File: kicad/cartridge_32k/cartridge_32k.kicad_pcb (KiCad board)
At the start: 2 copper layers, 39 x 66 mm, 8 parts, among them J1 Card edge (87715-9106 mate), U1 ATF22V10C-7PX, U2 AT28C256-15PU, U3 AS7C256C-15PCN

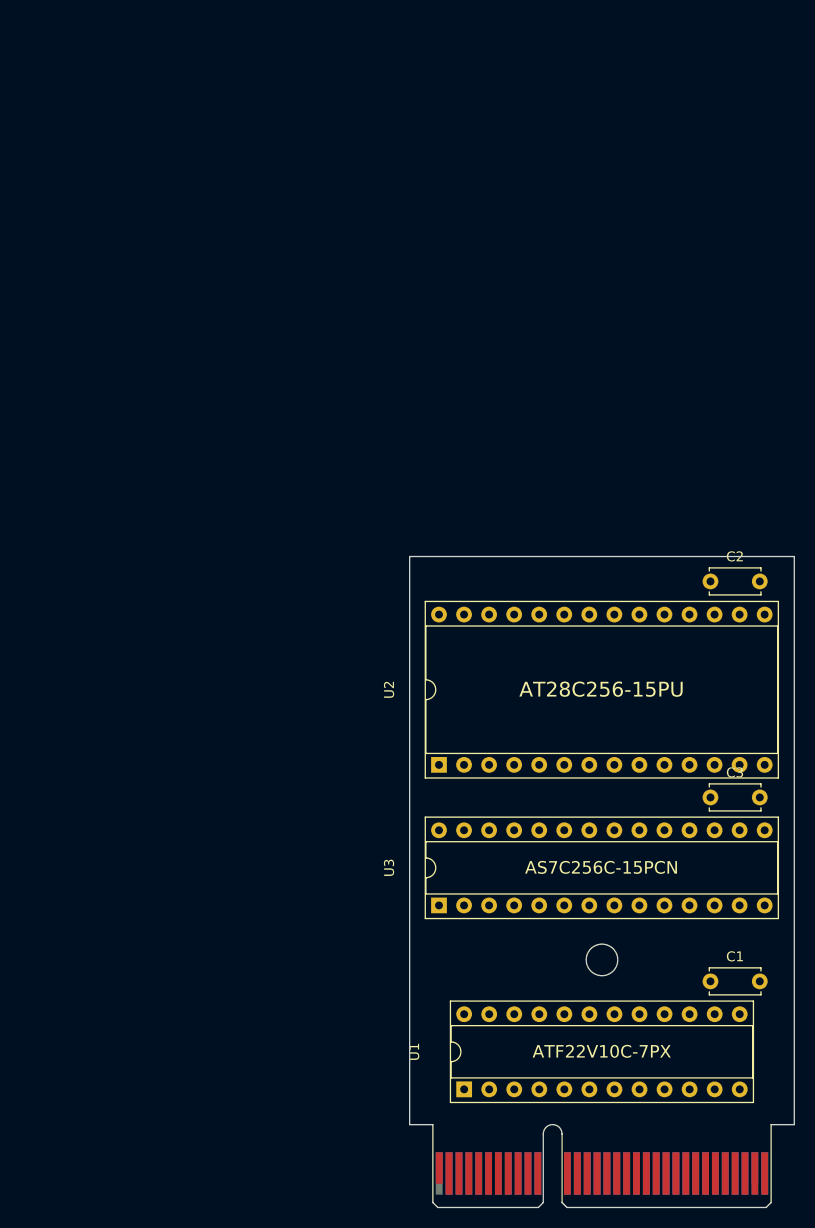
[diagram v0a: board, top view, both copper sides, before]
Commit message: 32K cartridge layout from Justin's local copy; main board zones refilled
- cartridge_32k: Justin's placement (J1, U1, U2, C1-C3, H1) and the
  KiCad 9 project settings it was saved with.
- placard.kicad_pcb: zones refilled in KiCad 9.0.6. 26 teardrops still
  carried the pre-#97 net names (SRC0-7, Net-(J8-/CART)); renamed to
  /Data bus/SRC0-7 and ~{CART} to match their net numbers. No footprint,
  track or via changes. DRC: only the 2 existing silk-over-copper warnings.

Co-Authored-By: Claude Opus 5.5 (1M context) <noreply@anthropic.com>
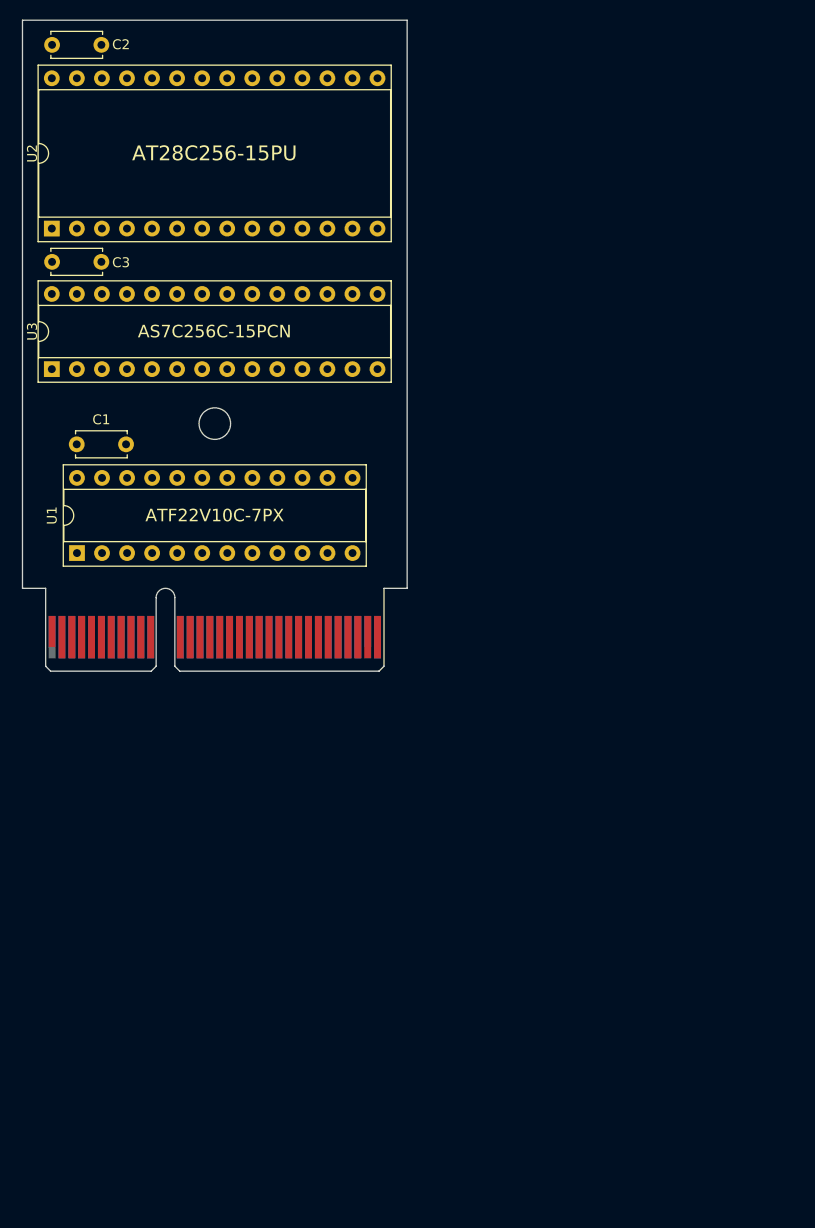
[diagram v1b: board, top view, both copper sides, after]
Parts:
- moved C2 86.1 mm to (63.7, 82.1)
- moved C3 86.1 mm to (63.7, 104.1)
- moved C1 84.2 mm to (66.2, 122.6)
- moved J1 67.1 mm to (63.7, 142.2)
- moved U1 67.1 mm to (66.3, 133.7)
- moved H1 67.1 mm to (80.2, 120.5)
- moved U2 67.1 mm to (63.7, 100.8)
- moved U3 67.1 mm to (63.7, 115.0)
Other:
- outline, holes or cut-outs redrawn

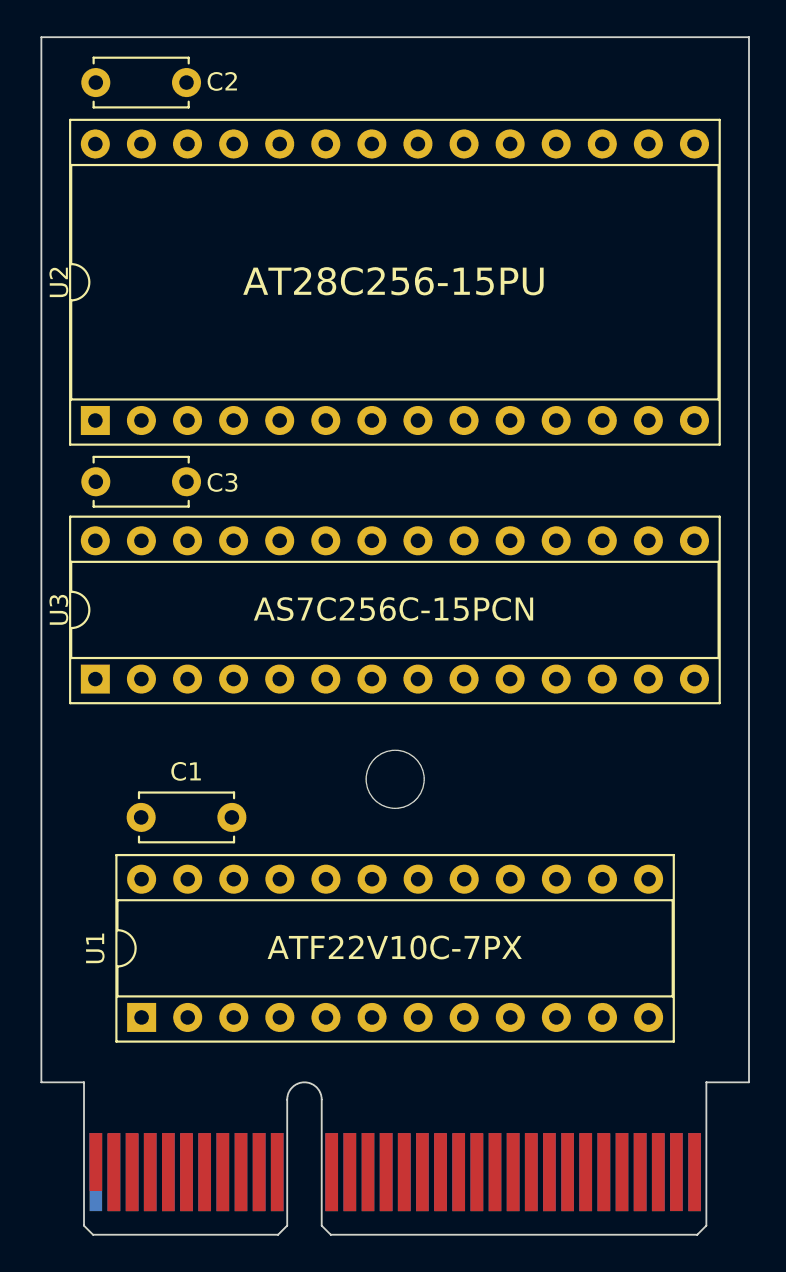
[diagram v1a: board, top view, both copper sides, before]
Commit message: Commit Justin's filled boards: routed carts, J8 reroute, J4 Hirose, library links
The three boards as Justin saved them after zone fill, teardrops and a
clean DRC (2026-10-26): both cartridges 4-layer routed, main board J8
rerouted for the new cartridge pinout, J4 swapped to the Hirose SD socket,
and every footprint linked to the placard library.

Co-Authored-By: Claude Opus 5.5 <noreply@anthropic.com>
Claude-Session: https://claude.ai/code/session_017okF1JiLRNFTfH7Az85hff
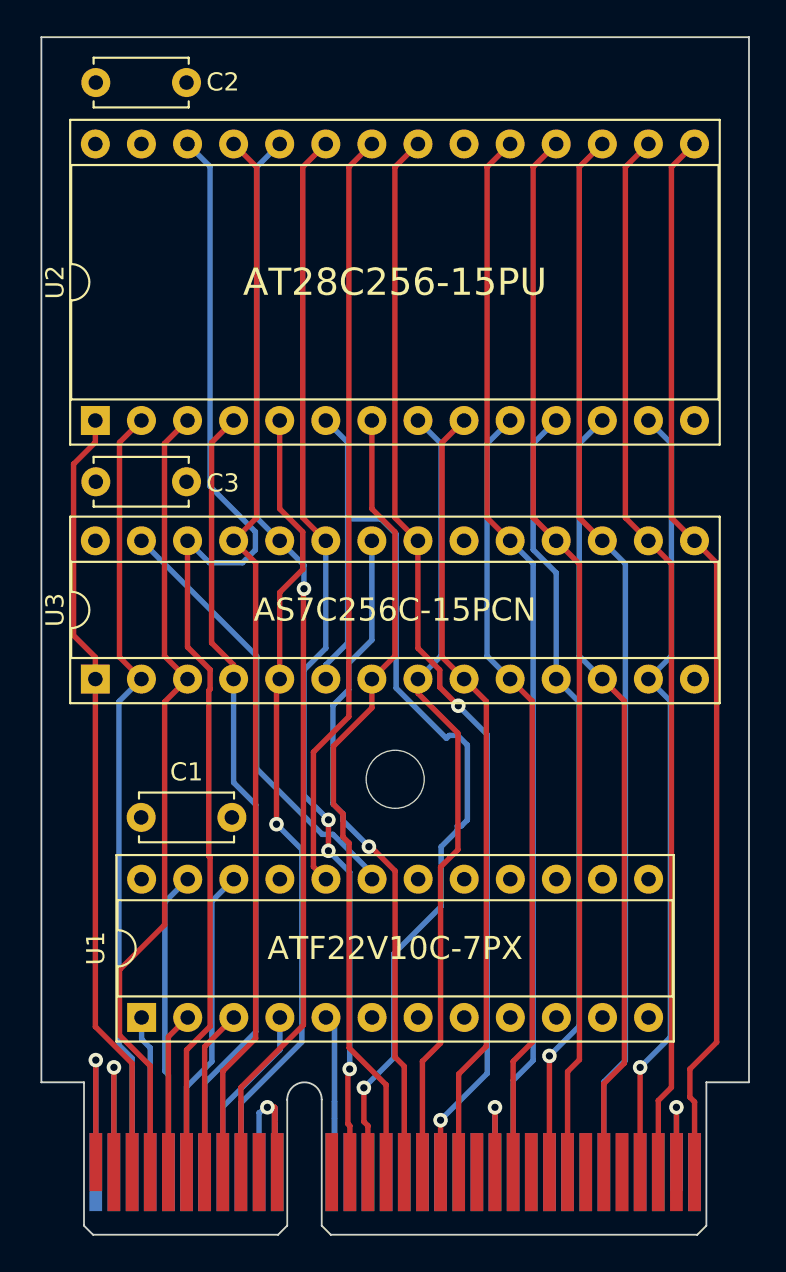
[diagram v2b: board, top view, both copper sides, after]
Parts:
- C1, C2, C3: footprint Capacitor_THT:C_Disc_D5.0mm_W2.5mm_P5.00mm -> placard:C_Disc_D5.0mm_W2.5mm_P5.00mm
- H1: footprint MountingHole:MountingHole_3.2mm_M3 -> placard:MountingHole_3.2mm_M3
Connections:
- J1 pad A10: /A14 -> (no net)
- J1 pad A12: /D0 -> (no net)
- J1 pad A13: /D2 -> /A11
- J1 pad A14: /D4 -> /A4
- J1 pad A15: /D6 -> /A3
- J1 pad A16: /~{CE_LO} -> /~{ROM_OE}
- J1 pad A17: /~{ROM_OE} -> /A2
- J1 pad A18: Net-(J1-PIXEL_ENABLE) -> /A10
- J1 pad A19: Net-(J1-RUN) -> /A1
- J1 pad A20: Net-(J1-CLK) -> (no net)
- J1 pad A22: unconnected-(J1-spare-PadA22) -> /A0
- J1 pad A24: unconnected-(J1-spare-PadA24) -> /D0
- J1 pad A25: unconnected-(J1-spare-PadA25) -> /D6
- J1 pad A27: unconnected-(J1-spare-PadA27) -> /D1
- J1 pad A29: unconnected-(J1-spare-PadA29) -> /D2
- J1 pad A3: /A0 -> /A14
- J1 pad A30: unconnected-(J1-spare-PadA30) -> /D4
- J1 pad A32: unconnected-(J1-spare-PadA32) -> /D3
- J1 pad A4: /A2 -> /A7
- J1 pad A5: /A4 -> /~{CE_LO}
- J1 pad A6: /A6 -> /A13
- J1 pad A7: /A8 -> Net-(J1-PIXEL_ENABLE)
- J1 pad A8: /A10 -> /A8
- J1 pad A9: /A12 -> /A9
- J1 pad B12: /D1 -> Net-(J1-STALL_IN)
- J1 pad B13: /D3 -> (no net)
- J1 pad B14: /D5 -> (no net)
- J1 pad B15: /D7 -> (no net)
- J1 pad B17: Net-(J1-STALL_IN) -> (no net)
- J1 pad B18: Net-(J1-STALL_OUT) -> (no net)
- J1 pad B19: Net-(J1-PC_ENABLE) -> (no net)
- J1 pad B22: unconnected-(J1-spare-PadB22) -> /D7
- J1 pad B27: unconnected-(J1-spare-PadB27) -> /D5
- J1 pad B3: /A1 -> /A12
- J1 pad B4: /A3 -> Net-(J1-CLK)
- J1 pad B5: /A5 -> Net-(J1-STALL_OUT)
- J1 pad B6: /A7 -> Net-(J1-RUN)
- J1 pad B7: /A9 -> /A6
- J1 pad B8: /A11 -> Net-(J1-PC_ENABLE)
- J1 pad B9: /A13 -> /A5
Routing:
- net /A13: track 0.00 -> 64.4 mm
- net /A10: track 0.00 -> 60.4 mm, vias 0 -> 2
- net /A9: track 0.00 -> 59.7 mm, vias 0 -> 1
- net /A11: track 0.00 -> 59.3 mm, vias 0 -> 3
- net /A8: track 0.00 -> 59.0 mm
- net /D3: track 0.00 -> 58.9 mm
- net /D5: track 0.00 -> 58.7 mm
- net /D7: track 0.00 -> 58.7 mm
- net /D4: track 0.00 -> 58.5 mm
- net /D6: track 0.00 -> 58.5 mm
- net /A4: track 0.00 -> 58.2 mm, vias 0 -> 1
- net /A7: track 0.00 -> 44.7 mm
- net /A3: track 0.00 -> 44.6 mm
- net /A5: track 0.00 -> 44.5 mm, vias 0 -> 1
- net /A2: track 0.00 -> 44.2 mm
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- added copper zone on In2.Cu, net +5V
- added copper zone on In1.Cu, net GND
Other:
- copper layers 2 -> 4

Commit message: Boards rev A with part numbers PLC-1001/1002/1003 and an S/N box
Silk block on each board (main front by the logo, carts on side B under the
title): PLC-100x REV A, an S/N label and a 17 x 5.5 mm box for a sticker or
paint pen. Board title blocks rev A with the part numbers; schematic title
blocks rev A with PCB/assembly numbers (gen_kicad_schematic.py); BOM bare-PCB
lines carry PLC-100x rev A and assemblies PLC-200x (gen_bom.py).

Co-Authored-By: Claude Opus 5.5 <noreply@anthropic.com>
Claude-Session: https://claude.ai/code/session_01DnW5SVDcRaZyJAhMGzz1W1
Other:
- board text added: "PLC-1002 REV A"
- board text added: "S/N"
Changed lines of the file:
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@@
 	(title_block
 		(title "PLACARD ROM cartridge, 32K")
-		(date "2026-10-26")
-		(rev "1")
+		(date "2026-10-29")
+		(rev "A")
 		(comment 1 "Placed by src/scripts/gen_kicad_cart_pcb.py; not routed")
+		(comment 2 "PCB PLC-1002, assembly PLC-2002")
 	)
 	(layers
@@
 		(layer "Edge.Cuts")
 	)
+	(gr_text "PLC-1002 REV A"
+		(at 80.245 88.9 0)
+		(layer "B.SilkS")
+		(effects
+			(font
+				(size 1.5 1.5)
+				(thickness 0.225)
+			)
+			(justify mirror)
+		)
+	)
+	(gr_text "S/N"
+		(at 87.045 93.55 0)
+		(layer "B.SilkS")
+		(effects
+			(font
+				(size 1.5 1.5)
+				(thickness 0.225)
+			)
+			(justify right mirror)
+		)
+	)
+	(gr_rect
+		(start 69.245 90.8)
+		(end 86.245 96.3)
+		(stroke
+			(width 0.15)
+			(type solid)
+		)
+		(fill no)
+		(layer "B.SilkS")
+	)
 	(gr_text "PLACARD ROM 32K"

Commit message: Carts: Justin's schematic update and refill, H1 restored; fab files regenerated
Update PCB from Schematic renamed the nets (ADDR*/DATABUS*), named the spare
fingers and added part fields, and removed the mounting hole H1 (not in the
cart schematics). H1 is put back at its old position (same uuid), zones
refilled. DRC 0/0/0. Copper otherwise unchanged; the 64K cart's stale plane
gap under U4 is now filled.

Co-Authored-By: Claude Opus 5.5 <noreply@anthropic.com>
Claude-Session: https://claude.ai/code/session_01DnW5SVfTC1ykqH1VEPPtnQ
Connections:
- net /A0 renamed /ADDR0
- net /A1 renamed /ADDR1
- net /A10 renamed /ADDR10
- net /A11 renamed /ADDR11
- net /A12 renamed /ADDR12
- net /A13 renamed /ADDR13
- net /A14 renamed /ADDR14
- net /A2 renamed /ADDR2
- net /A3 renamed /ADDR3
- net /A4 renamed /ADDR4
- net /A5 renamed /ADDR5
- net /A6 renamed /ADDR6
- net /A7 renamed /ADDR7
- net /A8 renamed /ADDR8
- net /A9 renamed /ADDR9
- net /D0 renamed /DATABUS0
- net /D1 renamed /DATABUS1
- net /D2 renamed /DATABUS2
- net /D3 renamed /DATABUS3
- net /D4 renamed /DATABUS4
- net /D5 renamed /DATABUS5
- net /D6 renamed /DATABUS6
- net /D7 renamed /DATABUS7
- J1 pad A10: (no net) -> unconnected-(J1-spare-PadA10)
- J1 pad A12: (no net) -> unconnected-(J1-spare-PadA12)
- J1 pad A20: (no net) -> unconnected-(J1-spare-PadA20)
- J1 pad B13: (no net) -> unconnected-(J1-spare-PadB13)
- J1 pad B14: (no net) -> unconnected-(J1-spare-PadB14)
- J1 pad B15: (no net) -> unconnected-(J1-spare-PadB15)
- J1 pad B17: (no net) -> unconnected-(J1-spare-PadB17)
- J1 pad B18: (no net) -> unconnected-(J1-spare-PadB18)
- J1 pad B19: (no net) -> unconnected-(J1-spare-PadB19)
